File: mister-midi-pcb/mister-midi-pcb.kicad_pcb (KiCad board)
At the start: 2 copper layers, 106.9 x 68.6 mm, 19 parts, among them J1 Midi In, J2 USB3_A, J3 Midi Out, J4 Midi Thru, U1 H11L1

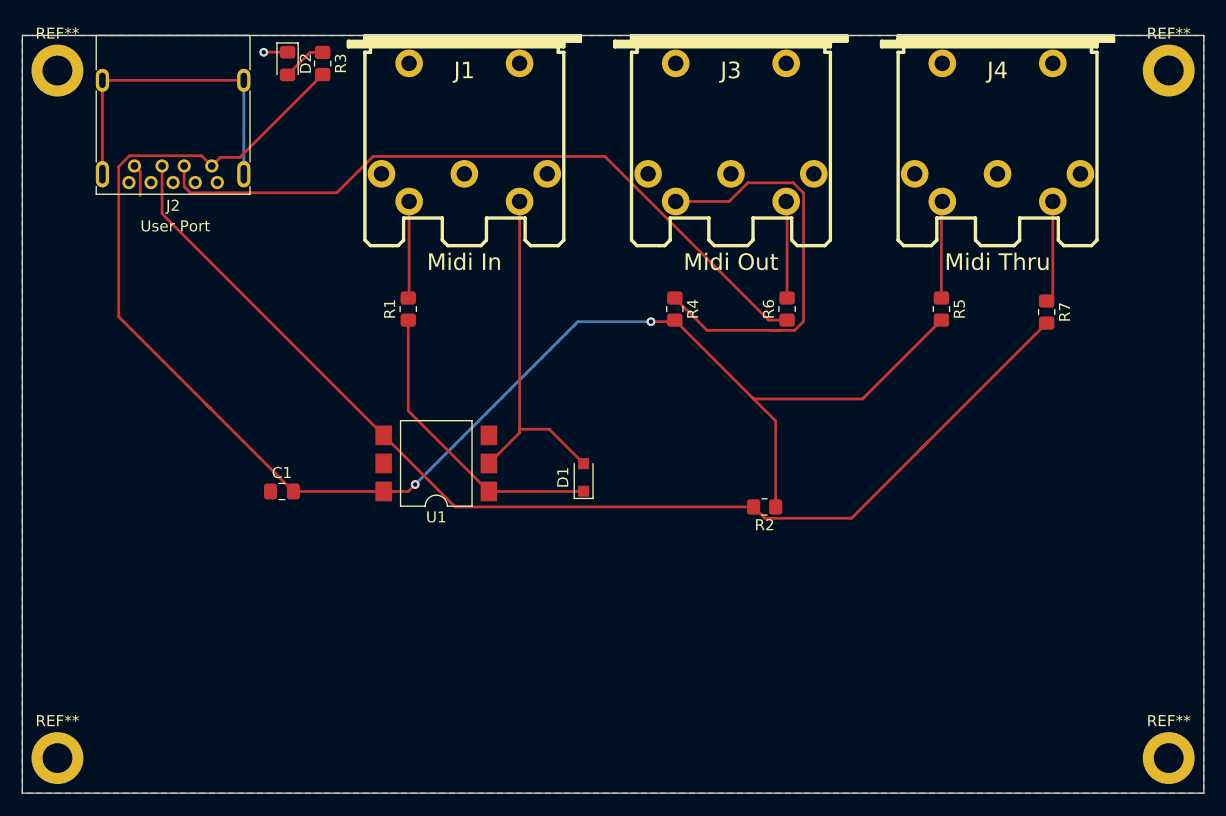
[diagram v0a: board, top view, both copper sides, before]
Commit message: reworked pcb with 3.3v
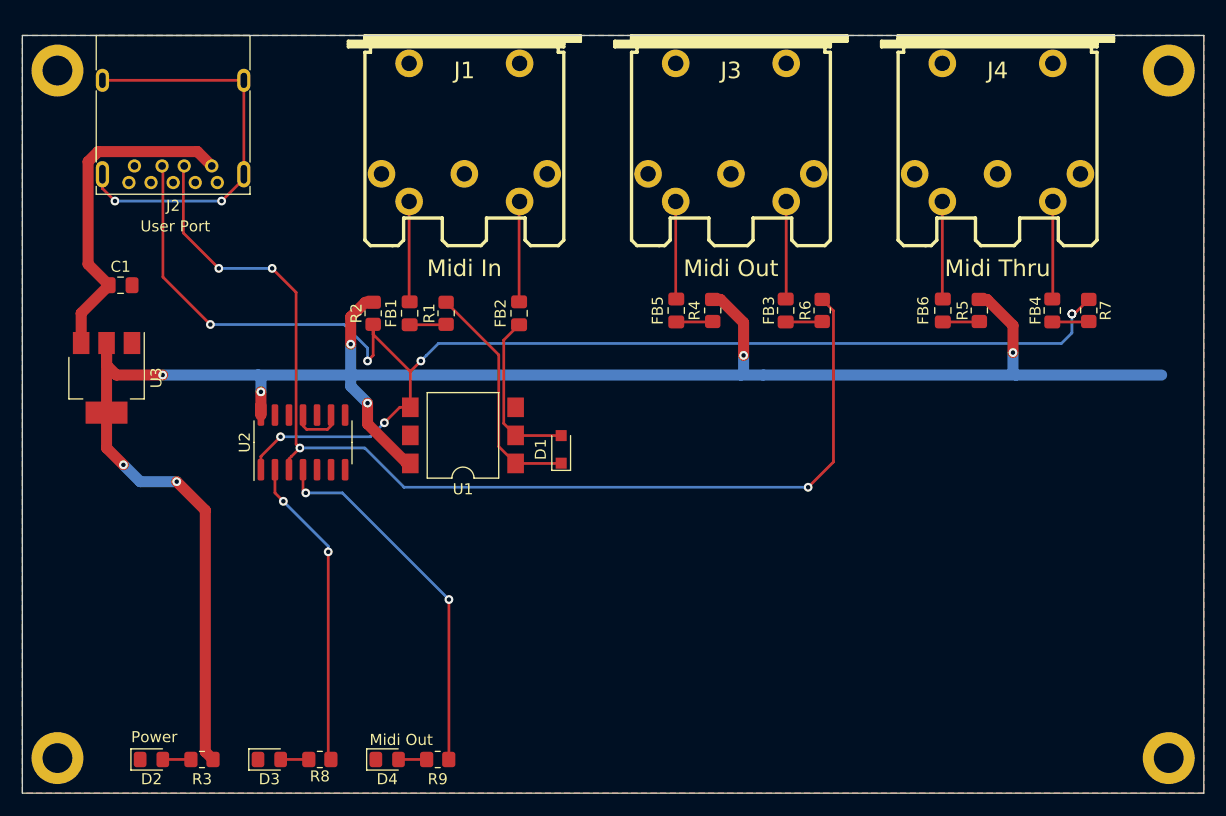
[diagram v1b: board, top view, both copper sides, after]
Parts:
- added D3: Blue LED, LED_SMD:LED_0805_2012Metric_Pad1.15x1.40mm_HandSolder, F.Cu at (83.3, 141.7)
- added D4: White LED, LED_SMD:LED_0805_2012Metric_Pad1.15x1.40mm_HandSolder, F.Cu at (94.0, 141.7)
- added FB1: Ferrite_Bead, Capacitor_SMD:C_0805_2012Metric_Pad1.18x1.45mm_HandSolder, F.Cu at (96.0, 101.3)
- added FB2: Ferrite_Bead, Capacitor_SMD:C_0805_2012Metric_Pad1.18x1.45mm_HandSolder, F.Cu at (105.9, 101.3)
- added FB3: Ferrite_Bead, Capacitor_SMD:C_0805_2012Metric_Pad1.18x1.45mm_HandSolder, F.Cu at (130.0, 101.1)
- added FB4: Ferrite_Bead, Capacitor_SMD:C_0805_2012Metric_Pad1.18x1.45mm_HandSolder, F.Cu at (154.2, 101.1)
- added FB5: Ferrite_Bead, Capacitor_SMD:C_0805_2012Metric_Pad1.18x1.45mm_HandSolder, F.Cu at (120.1, 101.1)
- added FB6: Ferrite_Bead, Capacitor_SMD:C_0805_2012Metric_Pad1.18x1.45mm_HandSolder, F.Cu at (144.3, 101.1)
- added R8: 2k, Resistor_SMD:R_0805_2012Metric_Pad1.20x1.40mm_HandSolder, F.Cu at (87.9, 141.7)
- added R9: 2k, Resistor_SMD:R_0805_2012Metric_Pad1.20x1.40mm_HandSolder, F.Cu at (98.6, 141.7)
- added U2: 74HC14, Package_SO:SO-14_3.9x8.65mm_P1.27mm, F.Cu at (86.4, 113.0)
- added U3: LM1117-3.3, Package_TO_SOT_SMD:SOT-223-3_TabPin2, F.Cu at (68.6, 107.2)
- D2: value LED -> Green LED
- R2: value 1k -> 470
- R3: value 220 -> 2k
- R4, R5: value 220 -> 33
- R6, R7: value 220 -> 10
- moved D2 64.2 mm to (72.6, 141.7), turned to 0 degrees
- moved R3 63.9 mm to (77.2, 141.7), turned to 0 degrees
- moved R2 39.5 mm to (92.7, 101.3), turned to 270 degrees
- moved C1 23.7 mm to (69.8, 98.8)
- moved R7 3.81 mm to (157.5, 101.1), turned to 90 degrees
- moved U1 3.50 mm to (100.8, 112.4)
- moved R1 3.45 mm to (99.3, 101.3), turned to 270 degrees
- moved R4 3.43 mm to (123.4, 101.1), turned to 90 degrees
- moved R5 3.43 mm to (147.6, 101.1), turned to 90 degrees
- moved D1 3.25 mm to (109.7, 113.7)
- moved R6 3.18 mm to (133.3, 101.1), turned to 270 degrees
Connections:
- C1 pad 1: GND -> +5V
- C1 pad 2: VCC -> GND
- J1 pad 4: Net-(J1-Pad4) -> Net-(FB1-Pad2)
- J1 pad 5: Net-(D1-Pad2) -> Net-(FB2-Pad2)
- J2 pad 1: VCC -> +5V
- J3 pad 4: Net-(J3-Pad4) -> Net-(FB5-Pad2)
- J3 pad 5: Net-(J3-Pad5) -> Net-(FB3-Pad1)
- J4 pad 4: Net-(J4-Pad4) -> Net-(FB6-Pad2)
- J4 pad 5: Net-(J4-Pad5) -> Net-(FB4-Pad1)
- R1 pad 2: Net-(J1-Pad4) -> Net-(FB1-Pad1)
- R2 pad 1: VCC -> +3V3
- R3 pad 2: VCC -> +3V3
- R4 pad 1: Net-(J3-Pad4) -> Net-(FB5-Pad1)
- R4 pad 2: VCC -> +3V3
- R5 pad 1: Net-(J4-Pad4) -> Net-(FB6-Pad1)
- R5 pad 2: VCC -> +3V3
- R6 pad 2: Net-(J3-Pad5) -> Net-(FB3-Pad2)
- R7 pad 1: Net-(J4-Pad5) -> Net-(FB4-Pad2)
- U1 pad 6: VCC -> +3V3
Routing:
- net +3V3: track 0.00 -> 182.0 mm, vias 0 -> 8
- net VCC: track 141.1 -> 0.00 mm, vias 2 -> 0
- net Net-(J3-Pad4): track 38.2 -> 0.00 mm
- net Midi_Out_TX: track 64.3 -> 101.0 mm, vias 0 -> 4
- net Midi_Out_TX_INV: track 0.00 -> 33.6 mm, vias 0 -> 2
- net +5V: track 0.00 -> 30.4 mm
- net Midi_In_RX_Inv: track 0.00 -> 28.3 mm, vias 0 -> 2
- net Midi_In_RX: track 104.1 -> 126.6 mm, vias 0 -> 7
- net Net-(D1-Pad2): track 31.9 -> 15.2 mm
- net Net-(J4-Pad5): track 9.35 -> 0.00 mm
- net Net-(FB1-Pad2): track 0.00 -> 9.10 mm
- net Net-(FB2-Pad2): track 0.00 -> 9.10 mm
- net Net-(FB6-Pad2): track 0.00 -> 8.85 mm
- net Net-(FB5-Pad2): track 0.00 -> 8.85 mm
- net Net-(FB4-Pad1): track 0.00 -> 8.85 mm
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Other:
- net class 3.3V / 5V added: clearance 0.2, trace_width 1, via_dia 0.8, via_drill 0.4
- board text added: "Midi Out"
- board text added: "Power"

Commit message: small fix.
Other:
- board text added: "Midi In"
- board text added: "Midi PCB for Mister v1.0"
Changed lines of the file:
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@@
   (general
     (thickness 1.6)
-    (drawings 7)
+    (drawings 9)
     (tracks 174)
     (zones 0)
@@
       (effects (font (size 1 1) (thickness 0.15)))
     )
-    (fp_text value 1N4148 (at 0.1 1.9 90) (layer F.Fab)
+    (fp_text value 1N4148 (at 0.1 1.9 90) (layer F.SilkS)
       (effects (font (size 1 1) (thickness 0.15)))
     )
@@
       (effects (font (size 1 1) (thickness 0.15)))
     )
-    (fp_text value H11L1 (at 0 4.87) (layer F.Fab)
+    (fp_text value H11L1 (at 0 4.87) (layer F.SilkS)
       (effects (font (size 1 1) (thickness 0.15)))
     )
@@
       (effects (font (size 1 1) (thickness 0.15)))
     )
-    (fp_text value 74HC14 (at 0 5.28 90) (layer F.Fab)
+    (fp_text value 74HC14 (at 0 5.28 90) (layer F.SilkS)
       (effects (font (size 1 1) (thickness 0.15)))
     )
@@
       (effects (font (size 1 1) (thickness 0.15)))
     )
-    (fp_text value LM1117-3.3 (at 0 4.5 90) (layer F.Fab)
+    (fp_text value LM1117-3.3 (at 0 4.5 90) (layer F.SilkS)
       (effects (font (size 1 1) (thickness 0.15)))
     )
@@
     )
   )
+  (gr_text "Midi In" (at 84.074 139.954) (layer F.SilkS)
+    (effects (font (size 1 1) (thickness 0.15)))
+  )
+  (gr_text "Midi PCB for Mister v1.0" (at 165.354 118.364 90) (layer F.SilkS)
+    (effects (font (size 2 2) (thickness 0.3)))
+  )
   (gr_text "Midi Out" (at 95.25 139.954) (layer F.SilkS)
